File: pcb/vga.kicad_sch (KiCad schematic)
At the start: 19 parts, among them J601 DB15_Female_HighDensity

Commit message: psu wiring and power cables
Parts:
- R606: value 8989 -> 17400; footprint Resistor_SMD:R_0805_2012Metric_Pad1.20x1.40mm_HandSolder -> Resistor_SMD:R_0603_1608Metric_Pad0.98x0.95mm_HandSolder
- R607: value 4495 -> 8760; footprint Resistor_SMD:R_0805_2012Metric_Pad1.20x1.40mm_HandSolder -> Resistor_SMD:R_0603_1608Metric_Pad0.98x0.95mm_HandSolder
- R608: value 2247 -> 4420; footprint Resistor_SMD:R_0805_2012Metric_Pad1.20x1.40mm_HandSolder -> Resistor_SMD:R_0603_1608Metric_Pad0.98x0.95mm_HandSolder
- R609: value 1124 -> 2200; footprint Resistor_SMD:R_0805_2012Metric_Pad1.20x1.40mm_HandSolder -> Resistor_SMD:R_0603_1608Metric_Pad0.98x0.95mm_HandSolder
- R610: value 562 -> 1300; footprint Resistor_SMD:R_0805_2012Metric_Pad1.20x1.40mm_HandSolder -> Resistor_SMD:R_0603_1608Metric_Pad0.98x0.95mm_HandSolder
- R611, R616: value 562 -> 550; footprint Resistor_SMD:R_0805_2012Metric_Pad1.20x1.40mm_HandSolder -> Resistor_SMD:R_0603_1608Metric_Pad0.98x0.95mm_HandSolder
- R612: value 8989 -> 8760; footprint Resistor_SMD:R_0805_2012Metric_Pad1.20x1.40mm_HandSolder -> Resistor_SMD:R_0603_1608Metric_Pad0.98x0.95mm_HandSolder
- R613: value 4495 -> 4420; footprint Resistor_SMD:R_0805_2012Metric_Pad1.20x1.40mm_HandSolder -> Resistor_SMD:R_0603_1608Metric_Pad0.98x0.95mm_HandSolder
- R614: value 2247 -> 2200; footprint Resistor_SMD:R_0805_2012Metric_Pad1.20x1.40mm_HandSolder -> Resistor_SMD:R_0603_1608Metric_Pad0.98x0.95mm_HandSolder
- R615: value 1124 -> 1300; footprint Resistor_SMD:R_0805_2012Metric_Pad1.20x1.40mm_HandSolder -> Resistor_SMD:R_0603_1608Metric_Pad0.98x0.95mm_HandSolder

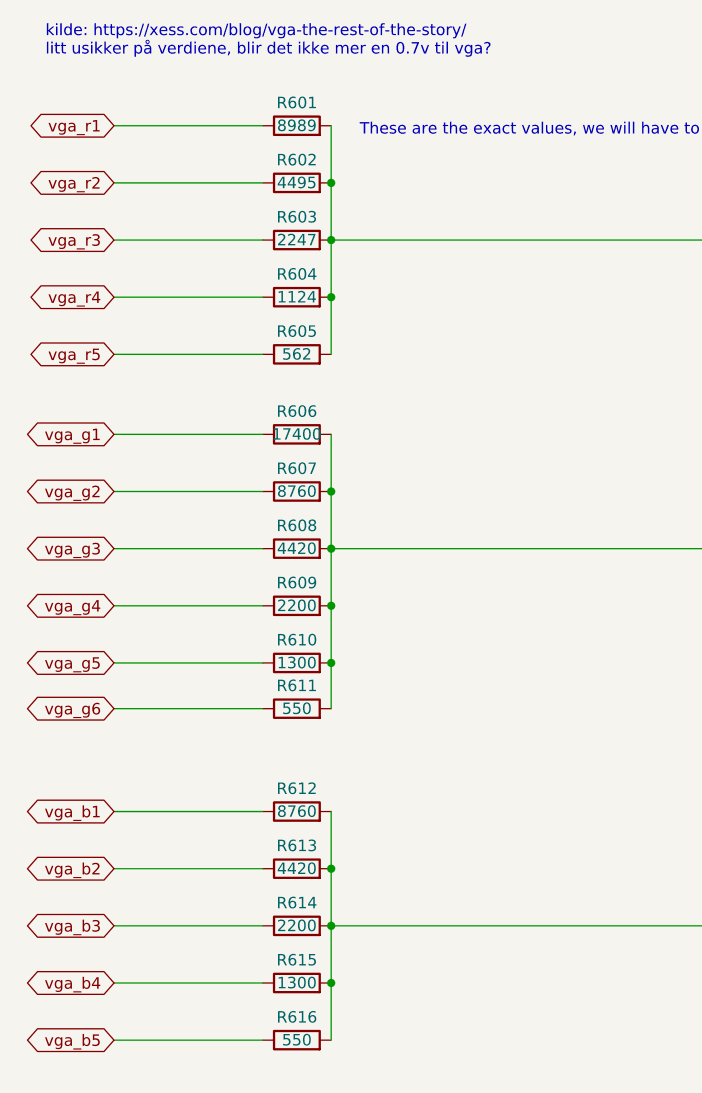
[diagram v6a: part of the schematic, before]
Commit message: add correct vga resistors
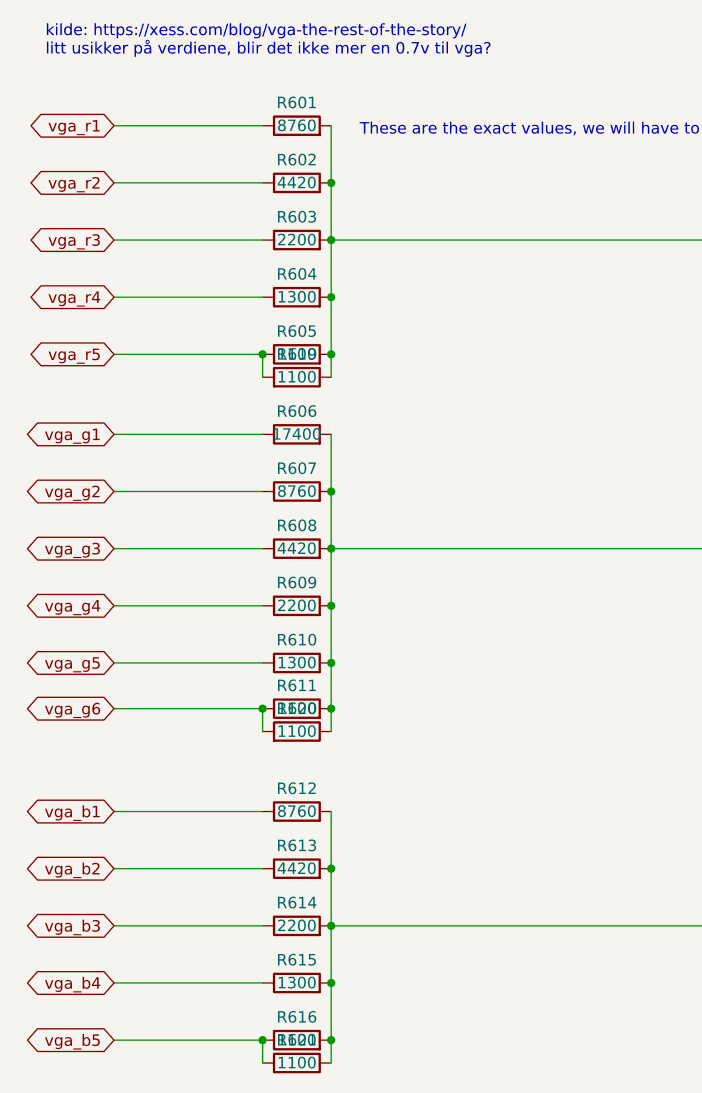
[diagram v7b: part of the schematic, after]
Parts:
- added R619, R620, R621: 1100, Resistor_SMD:R_0603_1608Metric_Pad0.98x0.95mm_HandSolder, symbol Device:R
- R601: value 8989 -> 8760; footprint Resistor_SMD:R_0805_2012Metric_Pad1.20x1.40mm_HandSolder -> Resistor_SMD:R_0603_1608Metric_Pad0.98x0.95mm_HandSolder
- R602: value 4495 -> 4420; footprint Resistor_SMD:R_0805_2012Metric_Pad1.20x1.40mm_HandSolder -> Resistor_SMD:R_0603_1608Metric_Pad0.98x0.95mm_HandSolder
- R603: value 2247 -> 2200; footprint Resistor_SMD:R_0805_2012Metric_Pad1.20x1.40mm_HandSolder -> Resistor_SMD:R_0603_1608Metric_Pad0.98x0.95mm_HandSolder
- R604: value 1124 -> 1300; footprint Resistor_SMD:R_0805_2012Metric_Pad1.20x1.40mm_HandSolder -> Resistor_SMD:R_0603_1608Metric_Pad0.98x0.95mm_HandSolder
- R605: value 562 -> 1100; footprint Resistor_SMD:R_0805_2012Metric_Pad1.20x1.40mm_HandSolder -> Resistor_SMD:R_0603_1608Metric_Pad0.98x0.95mm_HandSolder
- R611, R616: value 550 -> 1100
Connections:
- net vga_b5: now also R621.2
- net vga_g6: now also R620.2
- net vga_r5: now also R619.2
- net at J601.3, R612.2, R613.2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: now also R621.1
- net at J601.1, R601.2, R602.2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: now also R619.1
- net at J601.2, R606.2, R607.2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: now also R620.1

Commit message: fix capacitor values and footprints
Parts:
- R601, R607, R612: footprint Resistor_SMD:R_0603_1608Metric_Pad0.98x0.95mm_HandSolder -> Resistor_SMD:R_0805_2012Metric_Pad1.20x1.40mm_HandSolder
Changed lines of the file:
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@@
     (property "Reference" "R601" (id 0) (at 46.99 40.64 90))
     (property "Value" "8760" (id 1) (at 46.99 43.18 90))
-    (property "Footprint" "Resistor_SMD:R_0603_1608Metric_Pad0.98x0.95mm_HandSolder" (id 2) (at 46.99 44.958 90)
+    (property "Footprint" "Resistor_SMD:R_0805_2012Metric_Pad1.20x1.40mm_HandSolder" (id 2) (at 46.99 44.958 90)
       (effects (font (size 1.27 1.27)) hide)
     )
@@
     (property "Reference" "R612" (id 0) (at 46.99 116.84 90))
     (property "Value" "8760" (id 1) (at 46.99 119.38 90))
-    (property "Footprint" "Resistor_SMD:R_0603_1608Metric_Pad0.98x0.95mm_HandSolder" (id 2) (at 46.99 121.158 90)
+    (property "Footprint" "Resistor_SMD:R_0805_2012Metric_Pad1.20x1.40mm_HandSolder" (id 2) (at 46.99 121.158 90)
       (effects (font (size 1.27 1.27)) hide)
     )
@@
     (property "Reference" "R607" (id 0) (at 46.99 81.28 90))
     (property "Value" "8760" (id 1) (at 46.99 83.82 90))
-    (property "Footprint" "Resistor_SMD:R_0603_1608Metric_Pad0.98x0.95mm_HandSolder" (id 2) (at 46.99 85.598 90)
+    (property "Footprint" "Resistor_SMD:R_0805_2012Metric_Pad1.20x1.40mm_HandSolder" (id 2) (at 46.99 85.598 90)
       (effects (font (size 1.27 1.27)) hide)
     )
